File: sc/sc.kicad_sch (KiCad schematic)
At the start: 13 parts, among them SW1 SW_SPDT, U1 STM32F103C8Tx

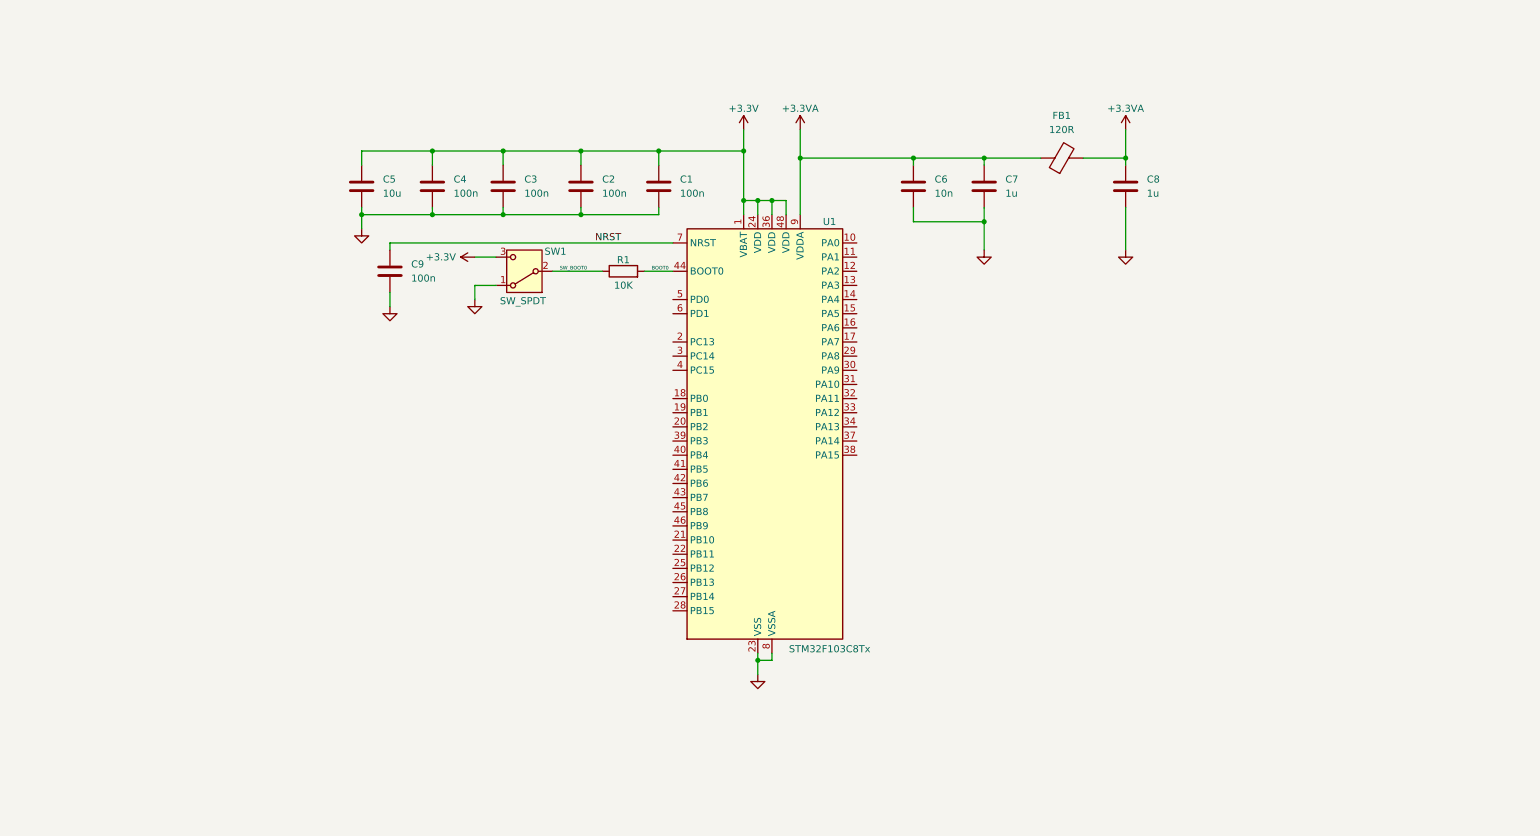
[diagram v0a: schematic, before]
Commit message: 3D view has been added
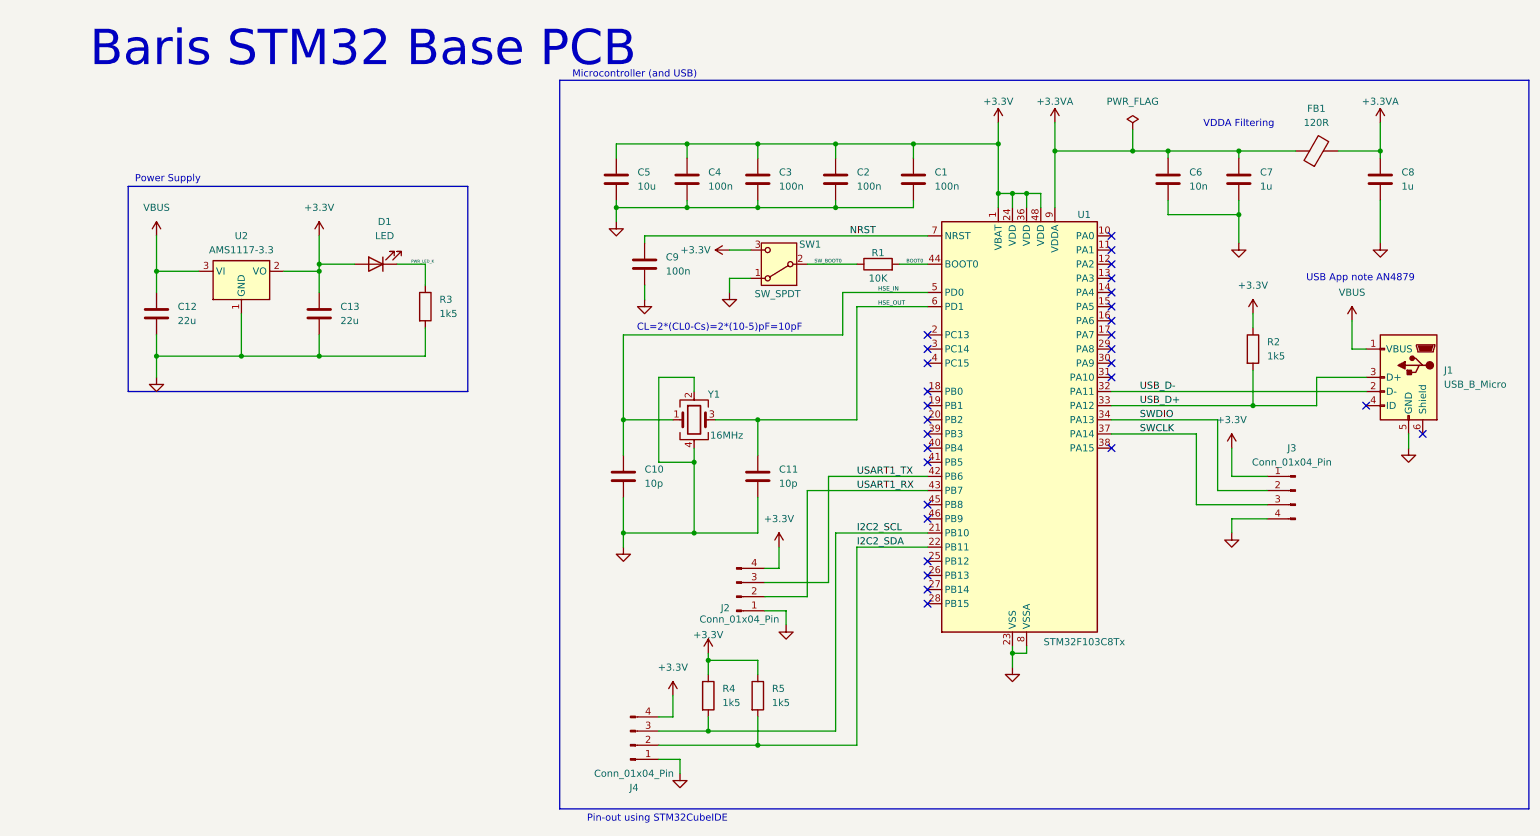
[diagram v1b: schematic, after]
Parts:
- added C10, C11: 10p, Capacitor_SMD:C_0402_1005Metric, symbol Device:C
- added C12, C13: 22u, Capacitor_SMD:C_0805_2012Metric, symbol Device:C
- added D1: LED, LED_SMD:LED_0603_1608Metric, symbol Device:LED
- added J1: USB_B_Micro, Connector_USB:USB_Micro-B_Wuerth_629105150521, symbol Connector:USB_B_Micro
- added J2, J3, J4: Conn_01x04_Pin, Connector_PinHeader_2.54mm:PinHeader_1x04_P2.54mm_Vertical, symbol Connector:Conn_01x04_Pin
- added R2, R3, R4, R5: 1k5, Resistor_SMD:R_0402_1005Metric, symbol Device:R
- added U2: AMS1117-3.3, Package_TO_SOT_SMD:SOT-223-3_TabPin2, symbol Regulator_Linear:AMS1117-3.3
- added Y1: 16MHz, Crystal:Crystal_SMD_3225-4Pin_3.2x2.5mm, symbol Device:Crystal_GND24
- C1, C2, C3, C4, C6, C7, C8, C9: footprint (none) -> Capacitor_SMD:C_0402_1005Metric
- C5: footprint (none) -> Capacitor_SMD:C_0603_1608Metric
- FB1: footprint (none) -> Inductor_SMD:L_0603_1608Metric
- R1: footprint (none) -> Resistor_SMD:R_0402_1005Metric
- SW1: footprint (none) -> Button_Switch_SMD:SW_SPDT_PCM12
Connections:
- net +3.3V: now also C13.1, D1.2 (A), J2.4 (Pin_4), J3.1 (Pin_1), J4.4 (Pin_4), R2.1, R4.1, R5.1, U2.2 (VO)
- net GND: now also C10.2, C11.2, C12.2, C13.2, J1.5 (GND), J2.1 (Pin_1), J3.4 (Pin_4), J4.1 (Pin_1), R3.2, U2.1 (GND), Y1.2, Y1.4
- net I2C2_SCL: now reaches U1.21 (PB10)
- net I2C2_SCL: now also J4.3 (Pin_3), R4.2
- net I2C2_SDA: now reaches U1.22 (PB11)
- net I2C2_SDA: now also J4.2 (Pin_2), R5.2
- net USB_D-: now reaches U1.32 (PA11)
- net USB_D-: now also J1.2 (D-)
- net USB_D+: now reaches U1.33 (PA12)
- net USB_D+: now also J1.3 (D+), R2.2
- net SWDIO: now reaches U1.34 (PA13)
- net SWDIO: now also J3.2 (Pin_2)
- net SWCLK: now reaches U1.37 (PA14)
- net SWCLK: now also J3.3 (Pin_3)
- net USART1_TX: now reaches U1.42 (PB6)
- net USART1_TX: now also J2.3 (Pin_3)
- net USART1_RX: now reaches U1.43 (PB7)
- net USART1_RX: now also J2.2 (Pin_2)
- net HSE_IN: now reaches U1.5 (PD0)
- net HSE_IN: now also C10.1, Y1.1
- net HSE_OUT: now reaches U1.6 (PD1)
- net HSE_OUT: now also C11.1, Y1.3
- new net PWR_LED_K: D1.1 (K), R3.1
- new net VBUS: C12.1, J1.1 (VBUS), U2.3 (VI)
- no-connect marks 0 -> 29
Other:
- note added: "Baris STM32 Base PCB"
- note added: "CL=2*(CL0-Cs)=2*(10-5)pF=10pF"
- note added: "Microcontroller (and USB)"
- note added: "Pin-out using STM32CubeIDE"
- note added: "Power Supply"
- note added: "USB App note AN4879"
- note added: "VDDA Filtering"
- title: (none) -> STM32 Base PCB
- moved on the sheet: C1, C2, C3, C4, C5, C6, C7, C8, C9, FB1, R1, SW1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
